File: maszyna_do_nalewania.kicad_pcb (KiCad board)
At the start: 2 copper layers, 68 parts, among them J1 USB_C_Receptacle_USB2.0_16P, J2 SMA_RP, SW1 CHIP_EN, SW2 BTN1, SW3 BTN2, U1 ESP32-C3, U2 TPS562202, U3 LM7806_TO220, U4 AD623, Y1 40Mhz 10ppm

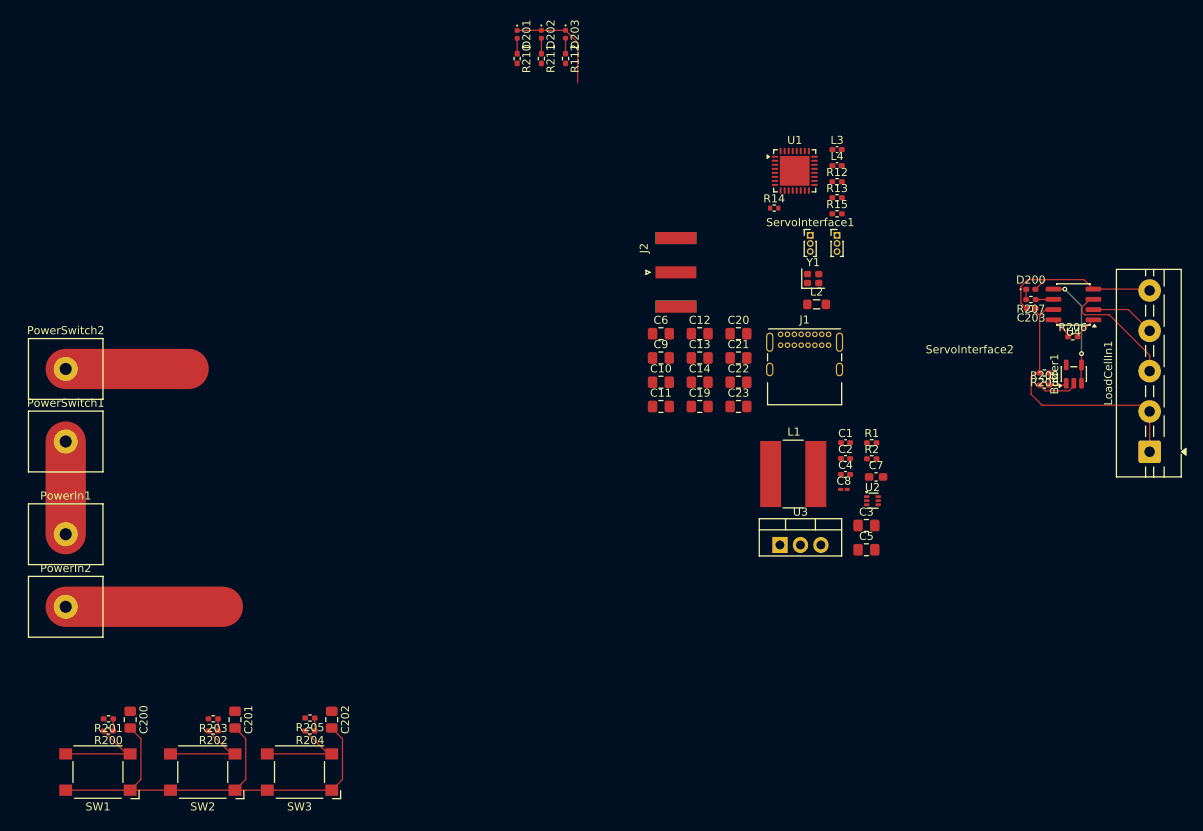
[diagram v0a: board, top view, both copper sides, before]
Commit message: feat: pcb almost done, added rgb led
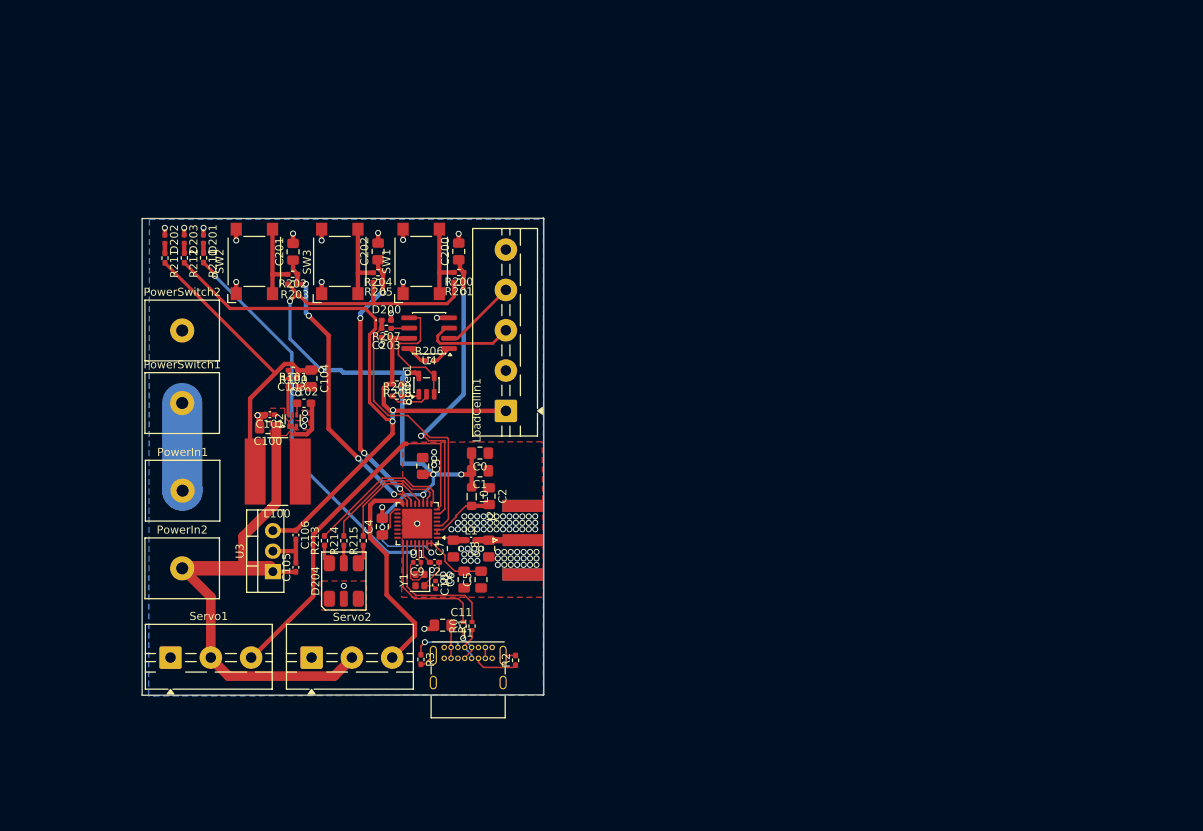
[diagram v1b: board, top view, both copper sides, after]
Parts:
- removed ServoInterface1: Servo1, Connector_PinHeader_1.00mm:PinHeader_1x03_P1.00mm_Vertical
- removed ServoInterface2: Servo2, Connector_PinHeader_1.00mm:PinHeader_1x03_P1.00mm_Vertical
- added D204: Inolux_IN-P55TATRGB, LED_SMD:LED_Inolux_IN-P55TATRGB_PLCC6_5.0x5.5mm_P1.8mm, F.Cu at (66.0, 86.8)
- added R213: 15Ohm, Resistor_SMD:R_0402_1005Metric_Pad0.72x0.64mm_HandSolder, F.Cu at (63.6, 81.8)
- added R214: 68Ohm, Resistor_SMD:R_0402_1005Metric_Pad0.72x0.64mm_HandSolder, F.Cu at (66.0, 81.8)
- added R215: 15Ohm, Resistor_SMD:R_0402_1005Metric_Pad0.72x0.64mm_HandSolder, F.Cu at (68.4, 81.8)
- added Servo1: ServoInterface1, TerminalBlock:TerminalBlock_MaiXu_MX126-5.0-03P_1x03_P5.00mm, F.Cu at (44.5, 96.3)
- added Servo2: ServoInterface2, TerminalBlock:TerminalBlock_MaiXu_MX126-5.0-03P_1x03_P5.00mm, F.Cu at (62.0, 96.3)
- C10: renamed from C20; footprint Capacitor_SMD:C_0805_2012Metric_Pad1.18x1.45mm_HandSolder -> Capacitor_SMD:C_0402_1005Metric
- C9: renamed from C19; footprint Capacitor_SMD:C_0805_2012Metric_Pad1.18x1.45mm_HandSolder -> Capacitor_SMD:C_0402_1005Metric
- R1: renamed from R15; footprint Resistor_SMD:R_0402_1005Metric_Pad0.72x0.64mm_HandSolder -> Resistor_SMD:R_0402_1005Metric
- moved Buffer1 80.3 mm to (76.3, 62.5)
- moved R208 80.3 mm to (72.6, 62.4)
- moved R209 80.3 mm to (72.6, 63.9)
- moved C203 80.1 mm to (71.2, 56.6)
- moved D200 80.0 mm to (71.3, 54.5)
- moved R207 80.0 mm to (71.3, 55.5)
- moved LoadCellIn1 80.0 mm to (86.1, 65.7)
- moved U4 80.0 mm to (76.6, 56.1)
- moved R206 79.9 mm to (76.6, 59.5)
- moved R3 78.6 mm to (75.6, 96.5), turned to -90 degrees
- moved C100 75.8 mm to (56.6, 67.8), turned to 180 degrees
- moved SW1 75.0 mm to (75.6, 47.2), turned to 90 degrees
- moved U2 72.6 mm to (59.7, 66.9), turned to 90 degrees
- moved R100 72.6 mm to (59.7, 60.7), turned to 180 degrees
- moved R101 72.1 mm to (59.7, 62.7)
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- renumbered C9 to C0, C10 to C1, C5 to C100, C2 to C101, C7 to C102, C8 to C103, C3 to C104, C1 to C105, C4 to C106, C21 to C11, C11 to C2, C6 to C3, C12 to C4, C14 to C5, C13 to C6, C22 to C7, C23 to C8, L2 to L0, L4 to L1, L1 to L100, L3 to L2, R14 to R0, R2 to R100, R1 to R101, R13 to R2, R112 to R212, R12 to R3
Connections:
- U1 pad 10: unconnected-(U1-MTDI-Pad10) -> /RGB_R
- U1 pad 12: unconnected-(U1-MTCK-Pad12) -> /RGB_G
- U1 pad 14: /BTN1 -> /BTN2
- U1 pad 15: /BTN2 -> /BTN1
- U1 pad 9: unconnected-(U1-MTMS-Pad9) -> /RGB_B
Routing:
- net +3V3: track 0.00 -> 153.7 mm, vias 0 -> 8
- net GND: track 115.6 -> 46.2 mm, vias 0 -> 103
- net +6V: track 34.2 -> 91.2 mm, vias 0 -> 2
- net /LED_INF: track 0.00 -> 50.0 mm, vias 0 -> 2
- net /Power/Bat+: track 19.5 -> 67.5 mm
- net /PWM_S1: track 0.00 -> 47.4 mm
- net /CHIP_EN: track 1.50 -> 37.3 mm, vias 0 -> 2
- net /BTN1: track 1.50 -> 37.2 mm, vias 0 -> 4
- net /BTN2: track 1.60 -> 34.5 mm, vias 0 -> 4
- net /LOAD_CELL: track 1.28 -> 33.4 mm
- net /PWM_S2: track 0.00 -> 26.9 mm
- net /RGB_B: track 0.00 -> 18.8 mm
- net /RGB_R: track 0.00 -> 16.7 mm
- net /USB_D+: track 0.00 -> 16.6 mm
- net /USB_D-: track 0.00 -> 16.0 mm
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- added copper zone on F.Cu, net /Power/Bat+
- added copper zone on B.Cu, net GND
- added copper zone on F.Cu, net GND
- added copper zone on F.Cu, net Net-(U2-SW)
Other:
- board outline added: 49.8 x 59.2 mm

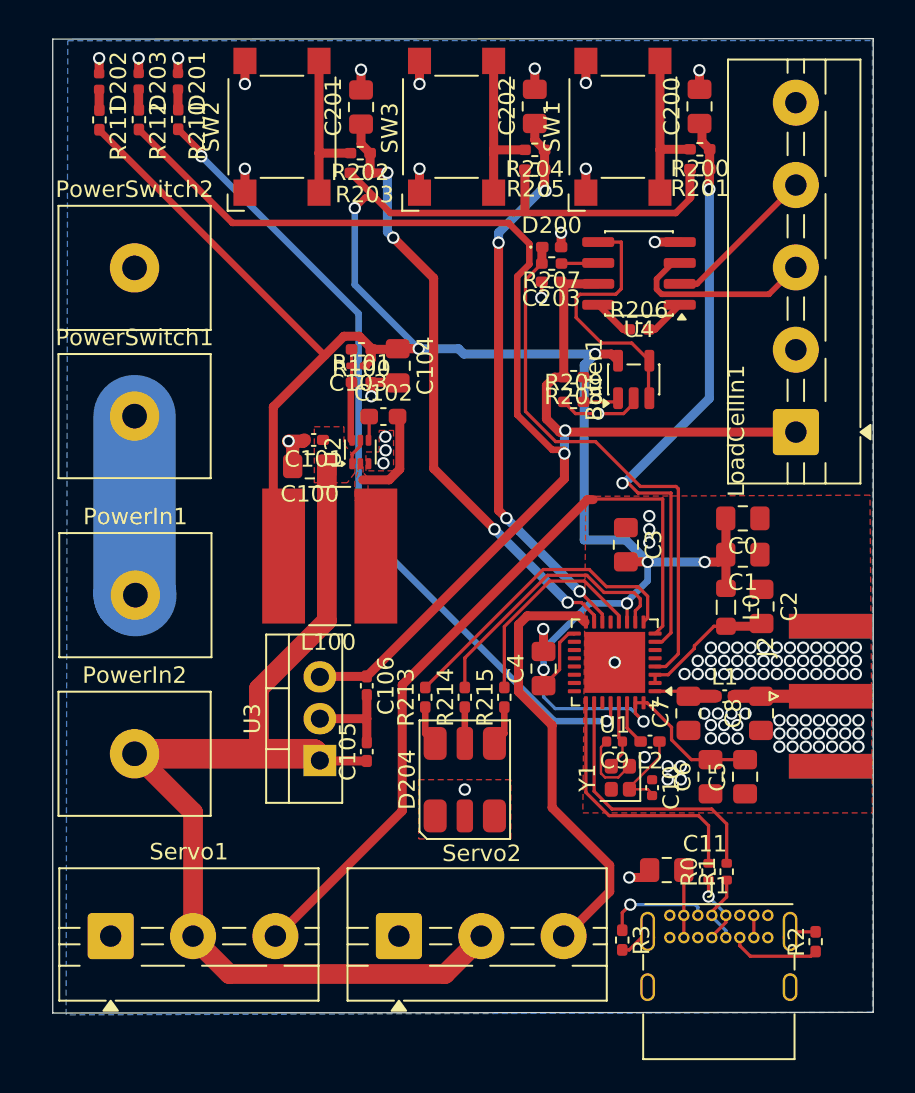
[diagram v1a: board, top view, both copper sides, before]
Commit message: feat: silkscreen done
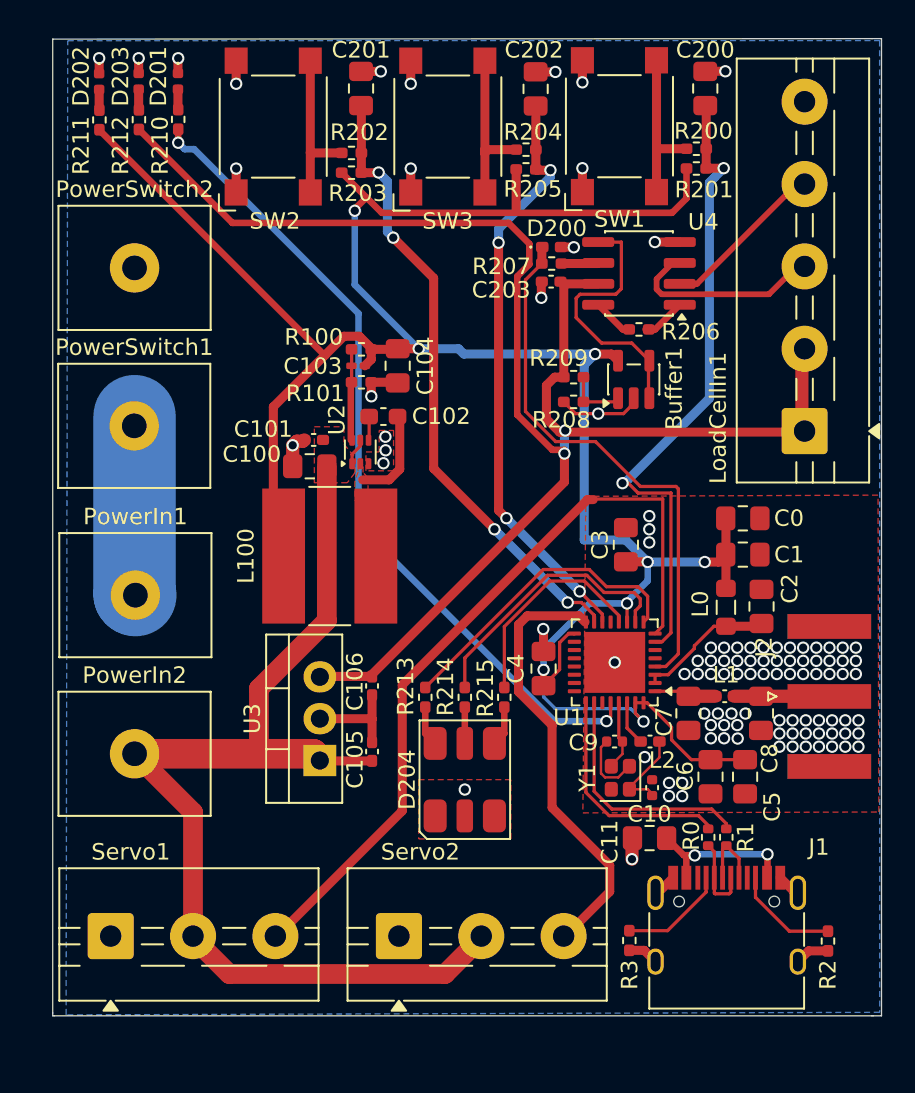
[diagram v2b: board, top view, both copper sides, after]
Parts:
- J1: footprint Connector_USB:USB_C_Receptacle_GCT_USB4085 -> Connector_USB:USB_C_Receptacle_HRO_TYPE-C-31-M-12
- moved J1 3.87 mm to (81.9, 96.8)
- moved C11 2.20 mm to (77.2, 90.3)
- moved R0 2.09 mm to (80.8, 90.3)
- moved R1 2.09 mm to (81.9, 90.3)
- moved C200 1.14 mm to (80.6, 44.8)
- moved C201 1.12 mm to (59.7, 44.8)
- moved C202 1.06 mm to (70.3, 44.9)
- moved R2 0.75 mm to (88.0, 96.6), turned to -90 degrees
- moved PowerSwitch1 0.59 mm to (45.9, 65.3)
- moved LoadCellIn1 0.53 mm to (86.6, 65.6)
- moved R202 0.53 mm to (59.1, 48.8)
- moved R204 0.53 mm to (69.7, 48.5)
- moved R205 0.53 mm to (69.7, 49.8)
- moved SW2 0.53 mm to (54.4, 47.1)
- moved SW3 0.53 mm to (65.0, 47.1)
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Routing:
- net +6V: track 91.2 -> 96.7 mm
- net Net-(C11-Pad2): track 5.00 -> 9.39 mm, vias 0 -> 2
- net /USB_D-: track 16.0 -> 13.7 mm
- net /USB_D+: track 16.6 -> 14.5 mm
- net GND: track 46.2 -> 48.2 mm
- net /CHIP_EN: track 37.3 -> 39.1 mm
- net Net-(J1-CC2): track 5.48 -> 6.44 mm
- net /BTN2: track 34.5 -> 35.5 mm
- net Net-(J1-D--PadA7): track 4.17 -> 4.96 mm, vias 1 -> 0
- net /BTN1: track 37.2 -> 37.8 mm
- net Net-(J1-CC1): track 6.41 -> 6.51 mm, vias 1 -> 0
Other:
- board size 49.8 x 59.2 mm -> 50.3 x 59.3 mm

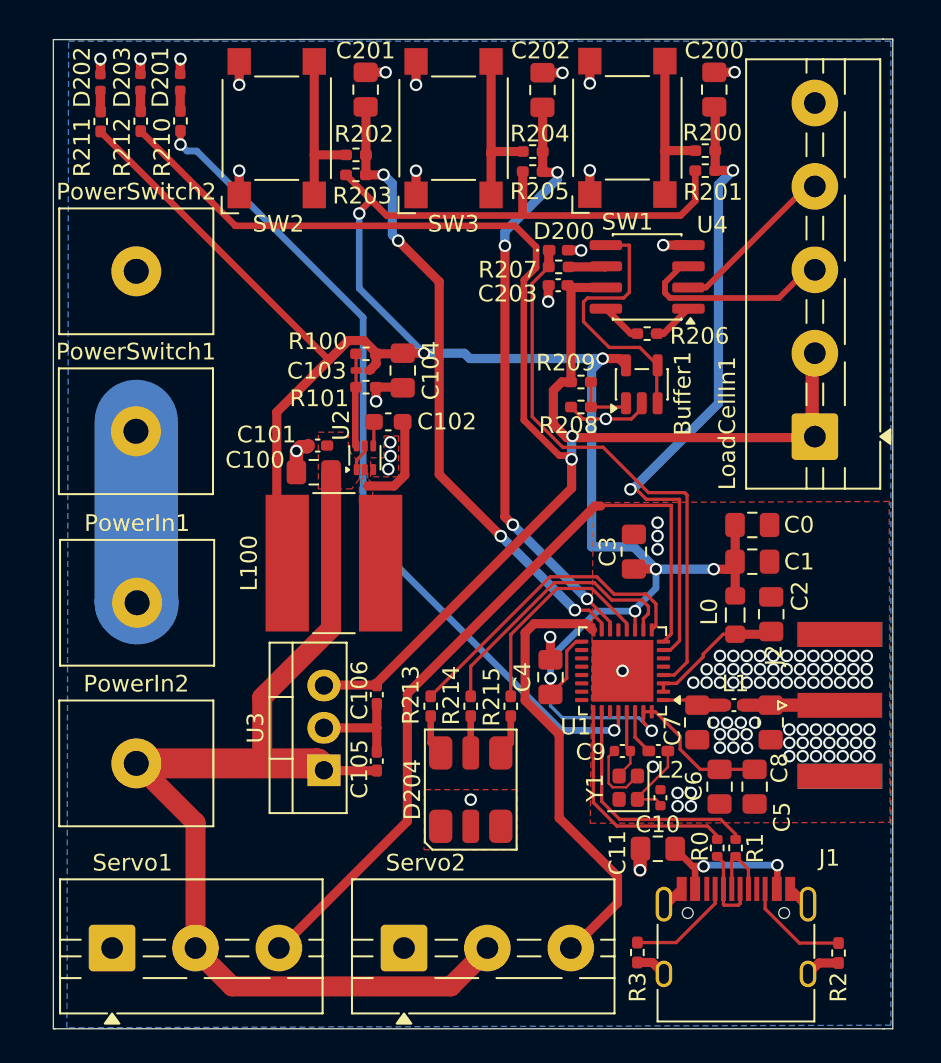
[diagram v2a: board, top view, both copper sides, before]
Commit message: fix: led resistor values, tensometer screw terminal
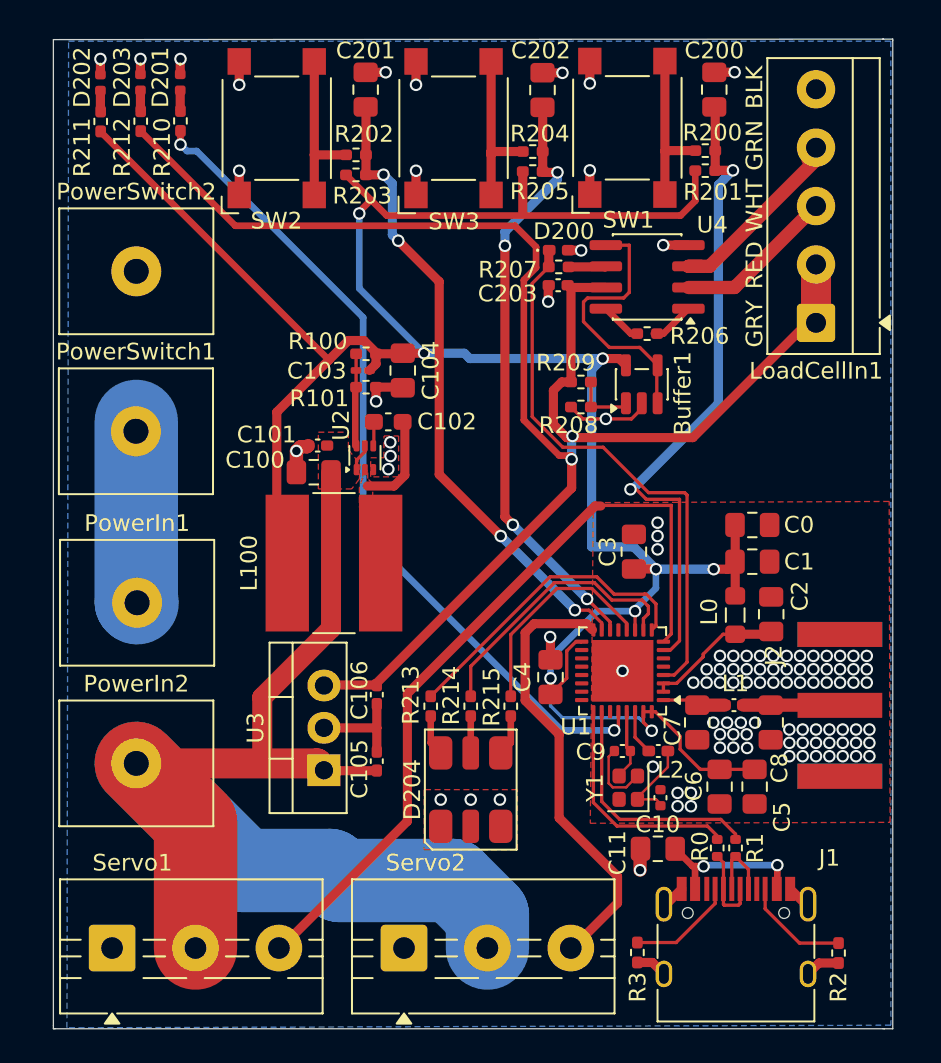
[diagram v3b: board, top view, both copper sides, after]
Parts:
- J2: value SMA_RP -> SMA
- LoadCellIn1: footprint TerminalBlock:TerminalBlock_MaiXu_MX126-5.0-05P_1x05_P5.00mm -> TerminalBlock_MetzConnect:TerminalBlock_MetzConnect_Type059_RT06305HBWC_1x05_P3.50mm_Horizontal
- R210, R211: value 65Ohm -> 68Ohm
- R212: value 65Ohm -> 200Ohm
- SW1, SW2, SW3: footprint Button_Switch_SMD:SW_SPST_Omron_B3FS-100xP -> Button_Switch_SMD:SW_SPST_Omron_B3FS-101xP
- moved LoadCellIn1 6.82 mm to (86.7, 58.8)
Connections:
- LoadCellIn1 pad 3: /Peripherals/GRN -> /Peripherals/WHT
- LoadCellIn1 pad 4: /Peripherals/WHT -> /Peripherals/GRN
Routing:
- net /Power/Bat+: track 67.8 -> 75.2 mm
- net +6V: track 96.7 -> 97.8 mm
- net /Peripherals/GRN: track 11.7 -> 12.2 mm
- net GND: vias 103 -> 105
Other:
- board text added: "BLK"
- board text added: "GRN"
- board text added: "GRY"
- board text added: "RED"
- board text added: "WHT"
